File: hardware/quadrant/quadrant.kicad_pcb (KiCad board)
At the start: 4 copper layers, 220 x 200 mm, 347 parts, among them J1 FPC 16, P1 NPTH, Q1 AO3401A, Q111 AO3400A, Q112 AO3401A, Q121 AO3400A, Q122 AO3401A, Q131 AO3400A, Q132 AO3401A, Q141 AO3400A, Q142 AO3401A, Q151 AO3400A, Q152 AO3401A, Q161 AO3400A, Q162 AO3401A, Q171 AO3400A, Q172 AO3401A, Q181 AO3400A, Q182 AO3401A, Q191 AO3400A, Q192 AO3401A, Q2 AO3400A, Q201 AO3400A, Q202 AO3401A, Q211 AO3400A, Q212 AO3401A, Q221 AO3400A, Q222 AO3401A, Q231 AO3400A, Q232 AO3401A, Q241 AO3400A, Q242 AO3401A, Q251 AO3400A, Q252 AO3401A, Q261 AO3400A, Q262 AO3401A, U1 74HC4514, U2 74HC154, U3 ADG1607, U4 ADG1607, U5 AD8421, U6 74LVC1G04, U7 OPA2810, U8 OPA2810

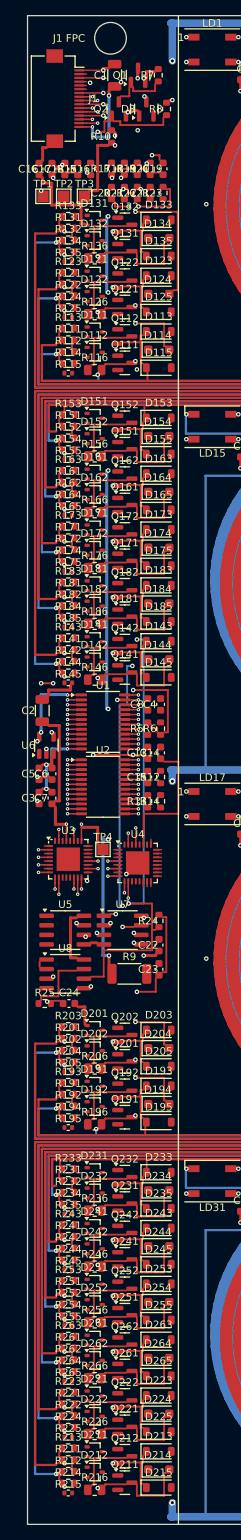
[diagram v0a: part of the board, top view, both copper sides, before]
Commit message: Cerveau fermé : haul VBAT, nets de liaison en premier, rip-up et reroutage, gerbers ; 4 x 4 régénéré et diagnostiqué
boardgen : rip-up et reroutage des nets murés à la fin du routage
(GenericBoard.reroute_walled) : un net en morceaux à la fois, ses
voisins à moins de 0,6 mm soulevés avec lui et reroutés, la levée
gardée si moins de nets restent en morceaux ; chaque piste et via se
souvient des lignes écrites dans le fichier de carte pour être levée ;
journal des levées imprimé par le build, BOARDGEN_RIP_UP=0 pour
comparer.

Cerveau : haul VBAT dessiné à la main sur la face arrière (bord sud,
colonne à l'ouest du lien puissance, montée au fusible F1) ; VBAT,
les quatre sorties analogiques et les deux lignes UART de l'isolateur
routés en premier ; chaque LED d'état à côté de sa résistance.
Résultat : 0 net ouvert, DRC KiCad sans élément non connecté ni
erreur, brain-gerbers.zip et empreinte commités, image régénérée.

Quadrant 4 x 4 : build du 20/09 commité (47 nets ouverts, 52 éléments
non connectés), diagnostic des trois champs d'échappées (multiplexeurs
LFCSP face à face, décodeurs à une rangée de vias, colonne
d'amplification) et plan des éventails à la main dans la note 04 ;
README, notes 07, 09 et 23 à jour.

Tests : l'archive du cerveau est attendue par les tests de gerbers et
par l'audit de fabrication.
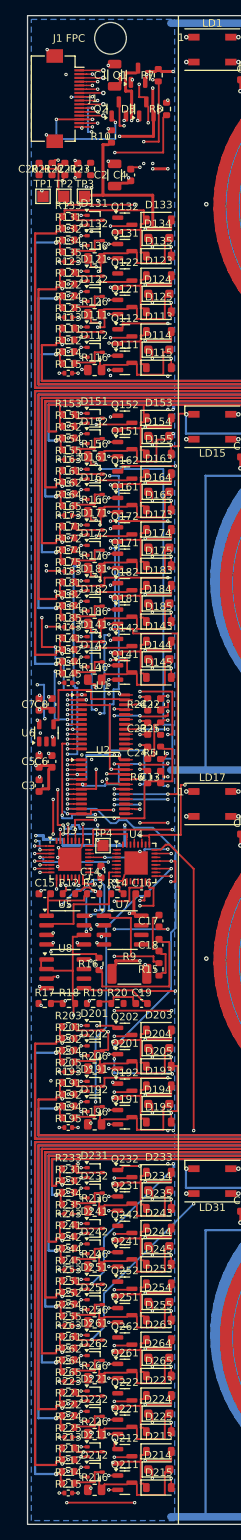
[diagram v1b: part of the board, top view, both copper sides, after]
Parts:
- moved R17 111.0 mm to (2.28, 131.0), turned to 0 degrees
- moved R18 110.9 mm to (5.49, 131.0), turned to 0 degrees
- moved R19 110.8 mm to (8.70, 131.0), turned to 0 degrees
- moved R20 110.7 mm to (11.9, 131.0), turned to 0 degrees
- moved C19 110.7 mm to (15.1, 131.0), turned to 0 degrees
- moved R15 106.6 mm to (17.4, 126.4)
- moved R16 105.4 mm to (9.48, 125.7)
- moved C18 103.6 mm to (17.4, 123.2)
- moved C17 100.7 mm to (17.4, 120.0)
- moved C16 97.0 mm to (15.1, 116.4), turned to 0 degrees
- moved C2 71.7 mm to (11.6, 21.1)
- moved C4 70.3 mm to (13.7, 21.1)
- moved R25 39.5 mm to (17.6, 94.5), turned to 90 degrees
- moved C24 34.8 mm to (15.9, 97.7), turned to 90 degrees
- moved C23 31.9 mm to (15.9, 94.5)
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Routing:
- net 5VA: track 212.8 -> 503.6 mm, vias 4 -> 47
- net VREF: track 214.0 -> 392.9 mm, vias 3 -> 41
- net DAMP1_N: track 1.84 -> 153.9 mm, vias 1 -> 11
- net MUX_A1: track 7.65 -> 139.5 mm, vias 4 -> 6
- net OUT_FB: track 124.7 -> 0.00 mm, vias 4 -> 0
- net MUX_EN_H: track 6.84 -> 124.8 mm, vias 3 -> 4
- net DRIVE1: track 1.84 -> 119.0 mm, vias 1 -> 10
- net MUX_A2: track 10.5 -> 126.3 mm, vias 5 -> 4
- net LP_OUT: track 122.4 -> 7.68 mm, vias 5 -> 0
- net LP_IN: track 112.6 -> 0.00 mm, vias 3 -> 0
- net MUX_A0: track 7.55 -> 119.5 mm, vias 3 -> 7
- net GND: track 2276.9 -> 2169.2 mm, vias 81 -> 189
- net MUX_EN_L: track 3.26 -> 110.6 mm, vias 2 -> 7
- net DAMP11_N: track 1.84 -> 101.6 mm, vias 1 -> 3
- net LP_FB: track 101.8 -> 4.29 mm
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- added copper zone on B.Cu, net GND

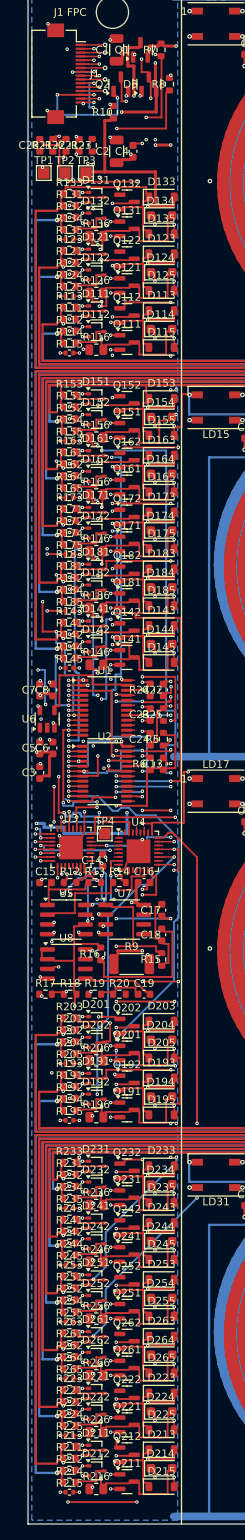
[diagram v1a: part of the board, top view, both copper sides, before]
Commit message: Quadrant 4 x 4 : build du 04/10 commité (24 nets ouverts au lieu de 47), le palier mesuré et documenté
Carte régénérée avec la configuration par défaut du générateur :
33171 segments, 946 vias, 15 raccords de la passe de finition, 24 nets
en morceaux, aucun défaut d'isolement ; DRC KiCad : 686 signalements,
31 éléments non connectés, aucune autre erreur. Image régénérée.

Ce qui reste ouvert : douze lignes de grille, neuf lignes M vers les
cellules lointaines, le retour du filtre vers l'étage de sortie, la
référence en huit pièces, un îlot de masse. Le compte des voies dans
les rangées de la dernière cellule de la bande 0 et sous les décodeurs
montre un écart de capacité, pas un défaut de recherche : les options
restantes (autoroutes à la main pour les cellules lointaines, bande de
24 mm, six couches, cellule allégée) sont des décisions de conception.

README du quadrant (plan de zone, résultat), notes 04 (le lot build par
build, les sondes, les options), 07 (état au 04/10), 09 (journal) et 23
(tableau des cartes et paragraphe du DRC) à jour. Toujours pas
d'archive de fabrication, le routage est ouvert.
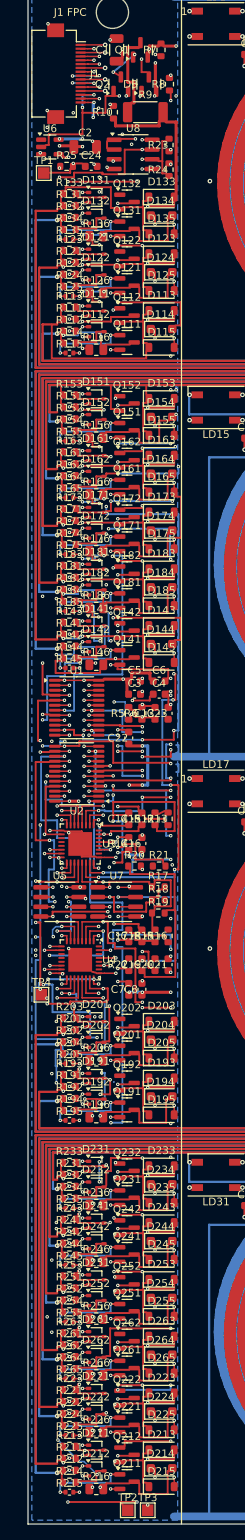
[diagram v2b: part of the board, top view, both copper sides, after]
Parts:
- moved TP2 174.4 mm to (13.0, 198.2)
- moved TP3 174.4 mm to (15.6, 198.2)
- moved R9 111.0 mm to (15.3, 16.0)
- moved C20 107.8 mm to (16.6, 127.1)
- moved C21 107.4 mm to (18.3, 127.1)
- moved R22 107.1 mm to (13.1, 127.1)
- moved U8 105.9 mm to (13.7, 21.5)
- moved R21 94.9 mm to (17.1, 114.3), turned to 0 degrees
- moved C24 75.0 mm to (8.24, 23.1), turned to 0 degrees
- moved U6 74.5 mm to (2.85, 20.6), turned to 0 degrees
- moved R25 72.5 mm to (5.03, 23.1), turned to 0 degrees
- moved C4 70.8 mm to (17.1, 91.9), turned to 0 degrees
- moved R24 67.8 mm to (18.4, 23.5)
- moved C7 40.7 mm to (13.1, 130.3)
- moved C8 40.7 mm to (14.8, 130.3)
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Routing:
- net M7_A: track 4.75 -> 126.7 mm, vias 0 -> 9
- net PULSE_RAIL: track 126.1 -> 9.70 mm, vias 2 -> 0
- net DAMP12_N: track 1.04 -> 109.5 mm, vias 0 -> 5
- net DRIVE16: track 11.8 -> 115.3 mm, vias 2 -> 6
- net DRIVE13: track 11.8 -> 113.3 mm, vias 2 -> 10
- net DRIVE9: track 11.8 -> 108.1 mm, vias 2 -> 7
- net M12_B: track 5.86 -> 97.2 mm, vias 0 -> 6
- net AMP_OUT: track 122.6 -> 33.8 mm, vias 5 -> 3
- net DAMP15_N: track 1.04 -> 87.5 mm, vias 0 -> 5
- net M6_A: track 4.90 -> 89.5 mm, vias 0 -> 8
- net DAMP14_N: track 1.04 -> 84.6 mm, vias 0 -> 5
- net M11_B: track 5.86 -> 85.9 mm, vias 0 -> 4
- net M5_A: track 86.9 -> 9.45 mm, vias 5 -> 1
- net M5_B: track 86.9 -> 10.4 mm, vias 7 -> 1
- net M16_B: track 5.71 -> 81.3 mm, vias 0 -> 4
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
